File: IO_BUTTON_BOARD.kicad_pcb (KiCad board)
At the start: 2 copper layers, 80 x 40 mm, 125 parts, among them P1 I2C, P10 IO_7, P2 I2C, P3 IO_0, P4 IO_1, P5 IO_2, P6 IO_3, P7 IO_4, P8 IO_5, P9 IO_6, Q1 NPN, Q10 PNP, Q11 PNP, Q12 PNP, Q13 PNP, Q2 PNP, Q3 NPN, Q4 PNP, Q5 NPN, Q6 PNP, Q7 PNP, Q8 PNP, Q9 PNP, SW1 I2C_ADDR, SW2 SW_0, SW3 SW_1, SW4 SW_2, SW5 SW_3, SW6 SW_4, SW7 SW_5, SW8 SW_6, SW9 SW_7, U1 PCF8574A, U2 74HC86, U3 74HC86

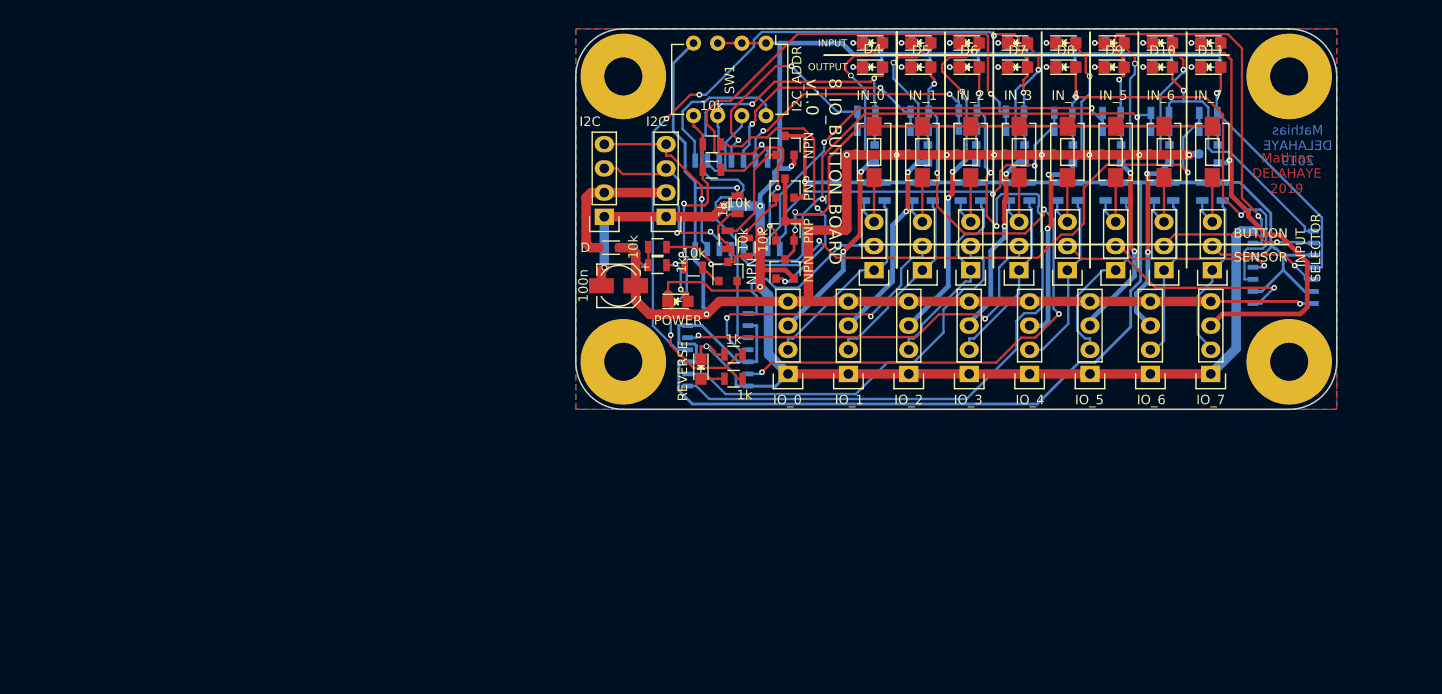
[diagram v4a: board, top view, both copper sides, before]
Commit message: Change Schematic with full separation of alimentations
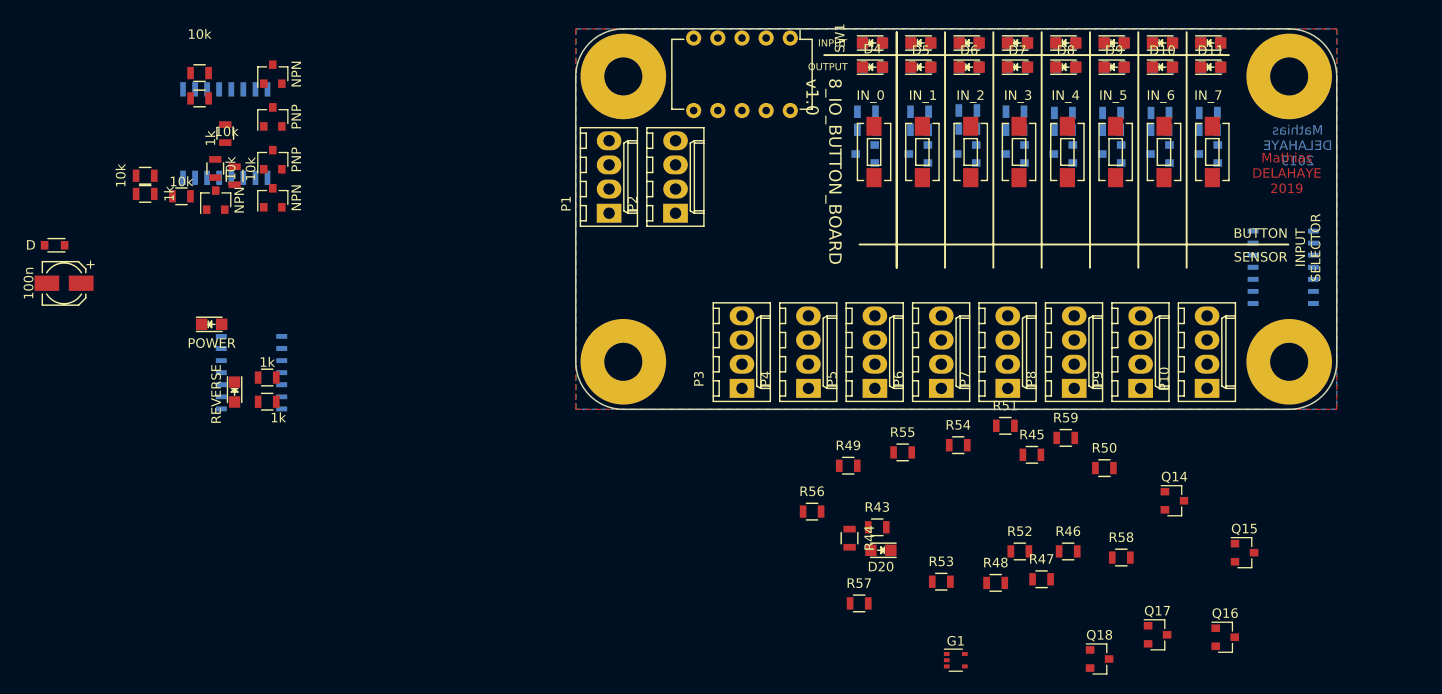
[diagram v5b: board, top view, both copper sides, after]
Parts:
- removed S1: IN_0, Pin_Headers:Pin_Header_Straight_1x03
- removed S2: IN_1, Pin_Headers:Pin_Header_Straight_1x03
- removed S3: IN_2, Pin_Headers:Pin_Header_Straight_1x03
- removed S4: IN_3, Pin_Headers:Pin_Header_Straight_1x03
- removed S5: IN_4, Pin_Headers:Pin_Header_Straight_1x03
- removed S6: IN_5, Pin_Headers:Pin_Header_Straight_1x03
- removed S7: IN_6, Pin_Headers:Pin_Header_Straight_1x03
- removed S8: IN_7, Pin_Headers:Pin_Header_Straight_1x03
- added D20: OUTPUT_MODE, LEDs:LED_0805, F.Cu at (132.1, 154.8)
- added G1: 74HC1G86GW, TO_SOT_Packages_SMD:SOT-353, F.Cu at (140.0, 166.4)
- added Q14: NPN, TO_SOT_Packages_SMD:SOT-23, F.Cu at (162.9, 149.6)
- added Q15: NPN, TO_SOT_Packages_SMD:SOT-23, F.Cu at (170.3, 155.1)
- added Q16: PNP, TO_SOT_Packages_SMD:SOT-23, F.Cu at (168.3, 164.0)
- added Q17: PNP, TO_SOT_Packages_SMD:SOT-23, F.Cu at (161.2, 163.7)
- added Q18: NPN, TO_SOT_Packages_SMD:SOT-23, F.Cu at (155.1, 166.2)
- added R59: 10k, Resistors_SMD:R_0805, F.Cu at (151.5, 143.0)
- P1, P10, P2, P3, P4, P5, P6, P7, P8, P9: footprint Pin_Headers:Pin_Header_Straight_1x04 -> Connectors_Molex:Molex_KK-6410-04_04x2.54mm_Straight
- R43, R44, R45, R46, R47, R48, R49, R51, R52, R53, R54, R55, R56, R57, R58: moved to F.Cu
- R50: value 1k -> 10k; moved to F.Cu
- SW1: value I2C_ADDR -> CONFIG; footprint Housings_DIP:DIP-8_W7.62mm -> Housings_DIP:DIP-10_W7.62mm
- moved C1 58.3 mm to (46.2, 126.7)
- moved D2 58.3 mm to (45.2, 122.7)
- moved R57 54.5 mm to (129.8, 160.4), turned to 0 degrees
- moved Q1 54.4 mm to (62.2, 118.0)
- moved Q2 54.4 mm to (68.2, 113.8)
- moved Q3 54.4 mm to (68.2, 117.8)
- moved Q4 54.4 mm to (68.2, 109.3)
- moved Q5 54.4 mm to (68.2, 104.8)
- moved R2 54.4 mm to (58.5, 117.6)
- moved R4 54.4 mm to (63.2, 111.0)
- moved R5 54.4 mm to (60.5, 107.3)
- moved R6 54.4 mm to (60.5, 104.6)
- moved R8 54.4 mm to (64.1, 115.4)
- moved U1 54.4 mm to (63.2, 111.0)
- moved R10 54.4 mm to (54.7, 115.4)
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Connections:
- Q10 pad 3: VCC -> /OUTPUT_VCC
- Q11 pad 3: VCC -> /OUTPUT_VCC
- Q12 pad 3: VCC -> /OUTPUT_VCC
- Q13 pad 3: VCC -> /OUTPUT_VCC
- Q6 pad 3: VCC -> /OUTPUT_VCC
- Q7 pad 3: VCC -> /OUTPUT_VCC
- Q8 pad 3: VCC -> /OUTPUT_VCC
- Q9 pad 3: VCC -> /OUTPUT_VCC
- R11 pad 2: GND -> /INPUT_LED_GND
- R12 pad 2: GND -> /INPUT_LED_GND
- R13 pad 2: GND -> /INPUT_LED_GND
- R14 pad 2: GND -> /INPUT_LED_GND
- R15 pad 2: GND -> /INPUT_LED_GND
- R16 pad 2: GND -> /INPUT_LED_GND
- R17 pad 2: GND -> /INPUT_LED_GND
- R18 pad 2: GND -> /INPUT_LED_GND
- R19 pad 2: GND -> /OUTPUT_LED_GND
- R20 pad 2: GND -> /OUTPUT_LED_GND
- R21 pad 2: GND -> /OUTPUT_LED_GND
- R22 pad 2: GND -> /OUTPUT_LED_GND
- R23 pad 2: GND -> /OUTPUT_LED_GND
- R24 pad 2: GND -> /OUTPUT_LED_GND
- R25 pad 2: GND -> /OUTPUT_LED_GND
- R26 pad 2: GND -> /OUTPUT_LED_GND
- R43 pad 1: /PULL_LANE -> /ACTIVE_OUTPUT
- R43 pad 2: Net-(R43-Pad2) -> GND
- R44 pad 1: /PULL_LANE -> /ACTIVE_OUTPUT
- R44 pad 2: Net-(R44-Pad2) -> Net-(D20-Pad2)
- R45 pad 1: /PULL_LANE -> /ACTIVE_OUTPUT
- R45 pad 2: Net-(R45-Pad2) -> Net-(Q14-Pad1)
- R46 pad 1: /PULL_LANE -> /ACTIVE_OUTPUT
- R46 pad 2: Net-(R46-Pad2) -> Net-(Q15-Pad1)
- R47 pad 1: /PULL_LANE -> Net-(Q16-Pad1)
- R47 pad 2: Net-(R47-Pad2) -> /ACTIVE_OUTPUT
- R48 pad 1: /PULL_LANE -> Net-(Q17-Pad1)
- R48 pad 2: Net-(R48-Pad2) -> Net-(Q15-Pad3)
- R49 pad 1: /PULL_LANE -> Net-(Q18-Pad1)
- R49 pad 2: Net-(R49-Pad2) -> Net-(Q16-Pad2)
- R50 pad 1: /PULL_LANE -> Net-(Q17-Pad1)
- R50 pad 2: Net-(R50-Pad2) -> VCC
- R51 pad 1: /IN_0 -> Net-(R51-Pad1)
- R52 pad 1: /IN_1 -> Net-(R52-Pad1)
- R53 pad 1: /IN_2 -> Net-(R53-Pad1)
- R54 pad 1: /IN_3 -> Net-(R54-Pad1)
- R55 pad 1: /IN_4 -> Net-(R55-Pad1)
- R56 pad 1: /IN_5 -> Net-(R56-Pad1)
- R57 pad 1: /IN_6 -> Net-(R57-Pad1)
- R58 pad 1: /IN_7 -> Net-(R58-Pad1)
- SW1 pad 5: /REVERSE_PULL -> VCC
- SW1 pad 6: Net-(SW1-Pad6) -> /ACTIVE_OUTPUT
- SW1 pad 7: Net-(SW1-Pad7) -> /REVERSE_PULL
- SW2 pad 2: Net-(R43-Pad2) -> Net-(S1-Pad3)
- SW3 pad 2: Net-(R44-Pad2) -> Net-(S2-Pad3)
- SW4 pad 2: Net-(R45-Pad2) -> Net-(S3-Pad3)
- SW5 pad 2: Net-(R46-Pad2) -> Net-(S4-Pad3)
- SW6 pad 2: Net-(R47-Pad2) -> Net-(S5-Pad3)
- SW7 pad 2: Net-(R48-Pad2) -> Net-(S6-Pad3)
- SW8 pad 2: Net-(R49-Pad2) -> Net-(S7-Pad3)
- SW9 pad 2: Net-(R50-Pad2) -> Net-(S8-Pad3)
- U1 pad 1: Net-(SW1-Pad8) -> Net-(SW1-Pad10)
- U1 pad 2: Net-(SW1-Pad7) -> Net-(SW1-Pad9)
- U1 pad 3: Net-(SW1-Pad6) -> Net-(SW1-Pad8)
- U2 pad 1: Net-(S1-Pad2) -> Net-(R51-Pad1)
- U2 pad 10: /PULL_LANE -> /REF_XOR
- U2 pad 12: Net-(S4-Pad2) -> Net-(R54-Pad1)
- U2 pad 13: /PULL_LANE -> /REF_XOR
- U2 pad 2: /PULL_LANE -> /REF_XOR
- U2 pad 4: Net-(S2-Pad2) -> Net-(R52-Pad1)
- U2 pad 5: /PULL_LANE -> /REF_XOR
- U2 pad 9: Net-(S3-Pad2) -> Net-(R53-Pad1)
- U3 pad 1: Net-(S5-Pad2) -> Net-(R55-Pad1)
- U3 pad 10: /PULL_LANE -> /REF_XOR
- U3 pad 12: Net-(S8-Pad2) -> Net-(R58-Pad1)
- U3 pad 13: /PULL_LANE -> /REF_XOR
- U3 pad 2: /PULL_LANE -> /REF_XOR
- U3 pad 4: Net-(S6-Pad2) -> Net-(R56-Pad1)
- U3 pad 5: /PULL_LANE -> /REF_XOR
- U3 pad 9: Net-(S7-Pad2) -> Net-(R57-Pad1)
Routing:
- net GND: track 233.5 -> 0.00 mm, vias 7 -> 0
- net VCC: track 197.1 -> 0.00 mm, vias 11 -> 0
- net /PULL_LANE: track 172.2 -> 0.00 mm, vias 1 -> 0
- net Net-(D6-Pad2): track 81.1 -> 0.00 mm, vias 3 -> 0
- net Net-(D7-Pad2): track 77.1 -> 0.00 mm, vias 4 -> 0
- net Net-(D5-Pad2): track 76.4 -> 0.00 mm, vias 5 -> 0
- net Net-(R27-Pad1): track 64.7 -> 0.00 mm, vias 2 -> 0
- net Net-(R28-Pad1): track 56.3 -> 0.00 mm, vias 2 -> 0
- net /CONTACT_LANE: track 56.3 -> 0.00 mm, vias 2 -> 0
- net Net-(R31-Pad1): track 56.1 -> 0.00 mm, vias 2 -> 0
- net Net-(D4-Pad2): track 56.0 -> 0.00 mm, vias 2 -> 0
- net Net-(R29-Pad1): track 47.0 -> 0.00 mm, vias 2 -> 0
- net Net-(D9-Pad2): track 46.1 -> 0.00 mm, vias 2 -> 0
- net /OUT_7: track 45.8 -> 0.00 mm, vias 1 -> 0
- net Net-(D8-Pad2): track 45.2 -> 0.00 mm, vias 2 -> 0
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
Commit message: Place mounting holes
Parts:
- removed Q18: NPN, TO_SOT_Packages_SMD:SOT-23
- removed REF01, REF02, REF03, REF04: MountingHole_4.3mm_M4, Mounting_Holes:MountingHole_4.3mm_M4
- added R60, R61, R62, R63, R64, R65, R66: 1k, Resistors_SMD:R_0805, F.Cu at (140.0, 150.1)
- added REF**: MountingHole_4mm, Mounting_Holes:MountingHole_4mm, F.Cu at (175.0, 135.0)
- added REF**: MountingHole_4mm, Mounting_Holes:MountingHole_4mm, F.Cu at (105.0, 135.0)
- added REF**: MountingHole_4mm, Mounting_Holes:MountingHole_4mm, F.Cu at (175.0, 105.0)
- added REF**: MountingHole_4mm, Mounting_Holes:MountingHole_4mm, F.Cu at (105.0, 105.0)
- D10: value IN_6 -> IN_5
- D11: value IN_7 -> IN_6
- D12: value OUT_0 -> IN_7
- D13: value OUT_1 -> OUT_0
- D14: value OUT_2 -> OUT_1
- D15: value OUT_3 -> OUT_2
- D16: value OUT_4 -> OUT_3
- D17: value OUT_5 -> OUT_4
- D18: value OUT_6 -> OUT_5
- D19: value OUT_7 -> OUT_6
- D20: value OUTPUT_MODE -> OUT_7
- D3: value POWER -> OUTPUT_MODE
- D4: value IN_0 -> POWER
- D5: value IN_1 -> IN_0
- D6: value IN_2 -> IN_1
- D7: value IN_3 -> IN_2
- D8: value IN_4 -> IN_3
- D9: value IN_5 -> IN_4
- Q14, Q15: value NPN -> PNP
- Q6, Q9: value PNP -> NPN
- R10, R35, R36, R37, R38, R39, R40, R41, R42, R59, R8, R9: value 10k -> 1k
- R11, R12, R13, R16, R17, R18, R43, R44, R45, R46, R47, R48, R49: value 1k -> 10k
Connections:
- D12 pad 2: /OUT_0 -> Net-(D12-Pad2)
- D13 pad 2: /OUT_1 -> /OUT_0
- D14 pad 2: /OUT_2 -> /OUT_1
- D15 pad 2: /OUT_3 -> /OUT_2
- D16 pad 2: /OUT_4 -> /OUT_3
- D17 pad 2: /OUT_5 -> /OUT_4
- D18 pad 2: /OUT_6 -> /OUT_5
- D19 pad 2: /OUT_7 -> /OUT_6
- D20 pad 1: GND -> Net-(D20-Pad1)
- D20 pad 2: Net-(D20-Pad2) -> /OUT_7
- D4 pad 1: Net-(D4-Pad1) -> GND
- P10 pad 2: /IN_7 -> (no net)
- P3 pad 2: /IN_0 -> (no net)
- P4 pad 2: /IN_1 -> (no net)
- P5 pad 2: /IN_2 -> (no net)
- P6 pad 2: /IN_3 -> (no net)
- P7 pad 2: /IN_4 -> (no net)
- P8 pad 2: /IN_5 -> (no net)
- P9 pad 2: /IN_6 -> (no net)
- Q10 pad 2: /OUT_4 -> /OUT_0
- Q11 pad 2: /OUT_5 -> /OUT_1
- Q12 pad 2: /OUT_6 -> /OUT_2
- Q13 pad 2: /OUT_7 -> /OUT_3
- Q14 pad 2: GND -> /OUT_4
- Q14 pad 3: /OUTPUT_LED_GND -> /OUTPUT_VCC
- Q15 pad 2: GND -> /OUT_5
- Q15 pad 3: Net-(Q15-Pad3) -> /OUTPUT_VCC
- Q16 pad 2: Net-(Q16-Pad2) -> /OUT_6
- Q16 pad 3: VCC -> /OUTPUT_VCC
- Q17 pad 2: /OUTPUT_VCC -> /OUT_7
- Q17 pad 3: VCC -> /OUTPUT_VCC
- Q6 pad 2: /OUT_0 -> GND
- Q6 pad 3: /OUTPUT_VCC -> Net-(Q6-Pad3)
- Q7 pad 2: /OUT_1 -> Net-(Q7-Pad2)
- Q7 pad 3: /OUTPUT_VCC -> VCC
- Q8 pad 2: /OUT_2 -> /OUTPUT_VCC
- Q8 pad 3: /OUTPUT_VCC -> VCC
- Q9 pad 2: /OUT_3 -> GND
- Q9 pad 3: /OUTPUT_VCC -> /INPUT_LED_GND
- R10 pad 1: Net-(R10-Pad1) -> /ACTIVE_OUTPUT
- R10 pad 2: VCC -> Net-(Q6-Pad1)
- R11 pad 1: Net-(D4-Pad1) -> Net-(Q7-Pad1)
- R11 pad 2: /INPUT_LED_GND -> /ACTIVE_OUTPUT
- R12 pad 1: Net-(D5-Pad1) -> Net-(Q4-Pad1)
- R12 pad 2: /INPUT_LED_GND -> Net-(Q1-Pad3)
- R13 pad 1: Net-(D6-Pad1) -> Net-(Q1-Pad3)
- R13 pad 2: /INPUT_LED_GND -> Net-(Q5-Pad1)
- R14 pad 1: Net-(D7-Pad1) -> Net-(Q8-Pad1)
- R14 pad 2: /INPUT_LED_GND -> Net-(Q6-Pad3)
- R15 pad 1: Net-(D8-Pad1) -> Net-(Q9-Pad1)
- R15 pad 2: /INPUT_LED_GND -> Net-(Q7-Pad2)
- R16 pad 1: Net-(D9-Pad1) -> Net-(Q8-Pad1)
- R16 pad 2: /INPUT_LED_GND -> VCC
- R17 pad 1: Net-(D10-Pad1) -> GND
- R17 pad 2: /INPUT_LED_GND -> Net-(Q9-Pad1)
- R18 pad 1: Net-(D11-Pad1) -> Net-(R18-Pad1)
- R18 pad 2: /INPUT_LED_GND -> VCC
- R19 pad 1: Net-(D12-Pad1) -> Net-(D5-Pad1)
- R19 pad 2: /OUTPUT_LED_GND -> /INPUT_LED_GND
- R20 pad 1: Net-(D13-Pad1) -> Net-(D6-Pad1)
- R20 pad 2: /OUTPUT_LED_GND -> /INPUT_LED_GND
- R21 pad 1: Net-(D14-Pad1) -> Net-(D7-Pad1)
- R21 pad 2: /OUTPUT_LED_GND -> /INPUT_LED_GND
- R22 pad 1: Net-(D15-Pad1) -> Net-(D8-Pad1)
- R22 pad 2: /OUTPUT_LED_GND -> /INPUT_LED_GND
- R23 pad 1: Net-(D16-Pad1) -> Net-(D9-Pad1)
- R23 pad 2: /OUTPUT_LED_GND -> /INPUT_LED_GND
- R24 pad 1: Net-(D17-Pad1) -> Net-(D10-Pad1)
- R24 pad 2: /OUTPUT_LED_GND -> /INPUT_LED_GND
- R25 pad 1: Net-(D18-Pad1) -> Net-(D11-Pad1)
- R25 pad 2: /OUTPUT_LED_GND -> /INPUT_LED_GND
- R26 pad 1: Net-(D19-Pad1) -> Net-(D12-Pad1)
- R26 pad 2: /OUTPUT_LED_GND -> /INPUT_LED_GND
- R27 pad 1: Net-(R27-Pad1) -> Net-(D13-Pad1)
- R27 pad 2: Net-(D11-Pad2) -> GND
- R28 pad 1: Net-(R28-Pad1) -> Net-(D14-Pad1)
- R28 pad 2: Net-(D10-Pad2) -> GND
- R29 pad 1: Net-(R29-Pad1) -> Net-(D15-Pad1)
- R29 pad 2: Net-(D9-Pad2) -> GND
- R30 pad 1: Net-(R30-Pad1) -> Net-(D16-Pad1)
- R30 pad 2: Net-(D8-Pad2) -> GND
- R31 pad 1: Net-(R31-Pad1) -> Net-(D17-Pad1)
- R31 pad 2: Net-(D7-Pad2) -> GND
- R32 pad 1: Net-(R32-Pad1) -> Net-(D18-Pad1)
- R32 pad 2: Net-(D6-Pad2) -> GND
- R33 pad 1: Net-(R33-Pad1) -> Net-(D19-Pad1)
- R33 pad 2: Net-(D5-Pad2) -> GND
- R34 pad 1: Net-(R34-Pad1) -> Net-(D20-Pad1)
- R34 pad 2: Net-(D4-Pad2) -> GND
- R35 pad 1: Net-(Q6-Pad1) -> Net-(R35-Pad1)
- R35 pad 2: Net-(R34-Pad1) -> Net-(D12-Pad2)
- R36 pad 1: Net-(Q7-Pad1) -> Net-(R36-Pad1)
- R36 pad 2: Net-(R33-Pad1) -> Net-(D11-Pad2)
- R37 pad 1: Net-(Q8-Pad1) -> Net-(R37-Pad1)
- R37 pad 2: Net-(R32-Pad1) -> Net-(D10-Pad2)
- R38 pad 1: Net-(Q9-Pad1) -> Net-(R38-Pad1)
- R38 pad 2: Net-(R31-Pad1) -> Net-(D9-Pad2)
- R39 pad 1: Net-(Q10-Pad1) -> Net-(R39-Pad1)
- R39 pad 2: Net-(R30-Pad1) -> Net-(D8-Pad2)
- R40 pad 1: Net-(Q11-Pad1) -> Net-(R40-Pad1)
- R40 pad 2: Net-(R29-Pad1) -> Net-(D7-Pad2)
- R41 pad 1: Net-(Q12-Pad1) -> Net-(R41-Pad1)
- R41 pad 2: Net-(R28-Pad1) -> Net-(D6-Pad2)
- R42 pad 1: Net-(Q13-Pad1) -> Net-(R42-Pad1)
- R42 pad 2: Net-(R27-Pad1) -> Net-(D5-Pad2)
- R43 pad 1: /ACTIVE_OUTPUT -> Net-(Q10-Pad1)
- R43 pad 2: GND -> Net-(R42-Pad1)
- R44 pad 1: /ACTIVE_OUTPUT -> Net-(Q11-Pad1)
- R44 pad 2: Net-(D20-Pad2) -> Net-(R41-Pad1)
- R45 pad 1: /ACTIVE_OUTPUT -> Net-(Q12-Pad1)
- R45 pad 2: Net-(Q14-Pad1) -> Net-(R40-Pad1)
- R46 pad 1: /ACTIVE_OUTPUT -> Net-(Q13-Pad1)
- R46 pad 2: Net-(Q15-Pad1) -> Net-(R39-Pad1)
- R47 pad 1: Net-(Q16-Pad1) -> Net-(Q14-Pad1)
- R47 pad 2: /ACTIVE_OUTPUT -> Net-(R38-Pad1)
- R48 pad 1: Net-(Q17-Pad1) -> Net-(Q15-Pad1)
- R48 pad 2: Net-(Q15-Pad3) -> Net-(R37-Pad1)
- R49 pad 1: Net-(Q18-Pad1) -> Net-(Q16-Pad1)
- R49 pad 2: Net-(Q16-Pad2) -> Net-(R36-Pad1)
- R50 pad 2: VCC -> Net-(R35-Pad1)
- R59 pad 1: GND -> Net-(R59-Pad1)
- R59 pad 2: Net-(Q18-Pad1) -> (no net)
- R7 pad 1: VCC -> /ACTIVE_OUTPUT
- R7 pad 2: Net-(D3-Pad2) -> GND
- R8 pad 1: Net-(Q4-Pad1) -> /ACTIVE_OUTPUT
- R8 pad 2: Net-(Q1-Pad3) -> Net-(D3-Pad2)
- R9 pad 1: Net-(Q1-Pad3) -> VCC
- R9 pad 2: Net-(Q5-Pad1) -> Net-(D4-Pad2)
- SW2 pad 1: /CONTACT_LANE -> Net-(R59-Pad1)
- SW2 pad 2: Net-(S1-Pad3) -> Net-(R51-Pad1)
- SW3 pad 1: /CONTACT_LANE -> Net-(R60-Pad1)
- SW3 pad 2: Net-(S2-Pad3) -> Net-(R52-Pad1)
- SW4 pad 1: /CONTACT_LANE -> Net-(R61-Pad1)
- SW4 pad 2: Net-(S3-Pad3) -> Net-(R53-Pad1)
- SW5 pad 1: /CONTACT_LANE -> Net-(R62-Pad1)
- SW5 pad 2: Net-(S4-Pad3) -> Net-(R54-Pad1)
- SW6 pad 1: /CONTACT_LANE -> Net-(R63-Pad1)
- SW6 pad 2: Net-(S5-Pad3) -> Net-(R55-Pad1)
- SW7 pad 1: /CONTACT_LANE -> Net-(R64-Pad1)
- SW7 pad 2: Net-(S6-Pad3) -> Net-(R56-Pad1)
- SW8 pad 1: /CONTACT_LANE -> Net-(R65-Pad1)
- SW8 pad 2: Net-(S7-Pad3) -> Net-(R57-Pad1)
- SW9 pad 1: /CONTACT_LANE -> Net-(R66-Pad1)
- SW9 pad 2: Net-(S8-Pad3) -> Net-(R58-Pad1)
- U1 pad 10: Net-(R29-Pad1) -> Net-(R37-Pad1)
- U1 pad 11: Net-(R28-Pad1) -> Net-(R36-Pad1)
- U1 pad 12: Net-(R27-Pad1) -> Net-(R35-Pad1)
- U1 pad 13: Net-(R10-Pad1) -> Net-(R18-Pad1)
- U1 pad 4: Net-(R34-Pad1) -> Net-(R42-Pad1)
- U1 pad 5: Net-(R33-Pad1) -> Net-(R41-Pad1)
- U1 pad 6: Net-(R32-Pad1) -> Net-(R40-Pad1)
- U1 pad 7: Net-(R31-Pad1) -> Net-(R39-Pad1)
- U1 pad 9: Net-(R30-Pad1) -> Net-(R38-Pad1)
- U2 pad 11: Net-(D7-Pad2) -> Net-(D8-Pad2)
- U2 pad 3: Net-(D4-Pad2) -> Net-(D5-Pad2)
- U2 pad 6: Net-(D5-Pad2) -> Net-(D6-Pad2)
- U2 pad 8: Net-(D6-Pad2) -> Net-(D7-Pad2)
- U3 pad 11: Net-(D11-Pad2) -> Net-(D12-Pad2)
- U3 pad 3: Net-(D8-Pad2) -> Net-(D9-Pad2)
- U3 pad 6: Net-(D9-Pad2) -> Net-(D10-Pad2)
- U3 pad 8: Net-(D10-Pad2) -> Net-(D11-Pad2)
